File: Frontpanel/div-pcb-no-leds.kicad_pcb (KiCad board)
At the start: 2 copper layers, 20 x 128.5 mm, 0 parts

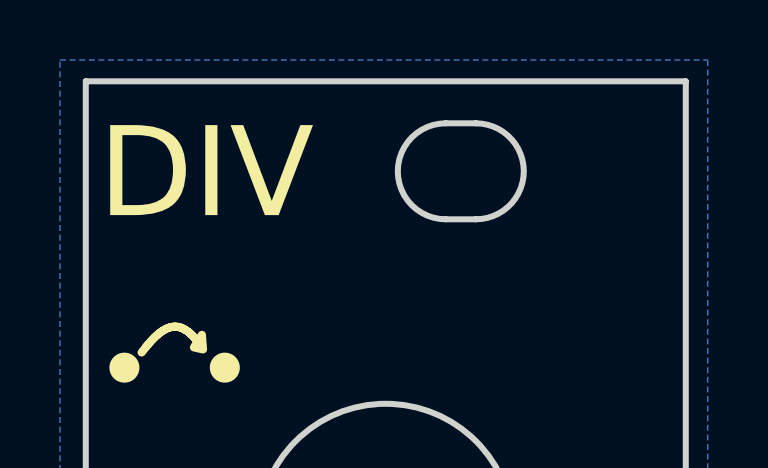
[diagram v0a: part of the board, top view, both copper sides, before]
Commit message: :lipstick: Change color of non-LED board and add "glow"
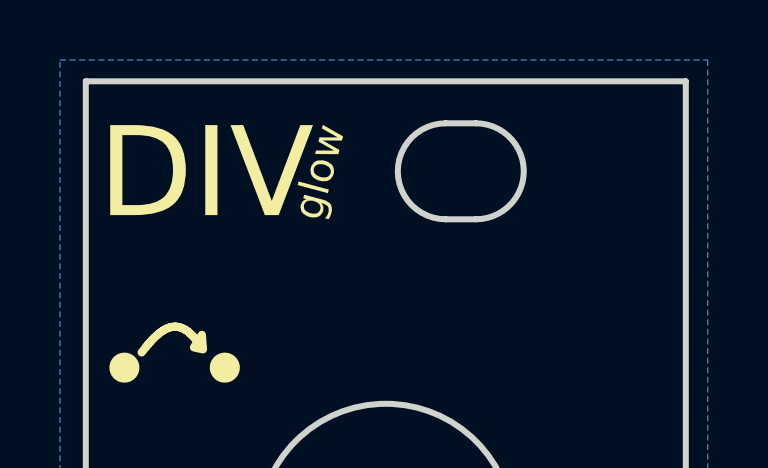
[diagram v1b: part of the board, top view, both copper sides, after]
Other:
- board text added: "glow"
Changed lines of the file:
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@@
   (setup
     (stackup
-      (layer "F.SilkS" (type "Top Silk Screen") (color "Black"))
+      (layer "F.SilkS" (type "Top Silk Screen") (color "White"))
       (layer "F.Paste" (type "Top Solder Paste"))
-      (layer "F.Mask" (type "Top Solder Mask") (color "White") (thickness 0.01))
+      (layer "F.Mask" (type "Top Solder Mask") (color "Black") (thickness 0.01))
       (layer "F.Cu" (type "copper") (thickness 0.035))
       (layer "dielectric 1" (type "core") (color "Polyimide") (thickness 1.51) (material "FR4") (epsilon_r 4.5) (loss_tangent 0.02))
       (layer "B.Cu" (type "copper") (thickness 0.035))
-      (layer "B.Mask" (type "Bottom Solder Mask") (color "White") (thickness 0.01))
+      (layer "B.Mask" (type "Bottom Solder Mask") (color "Black") (thickness 0.01))
       (layer "B.Paste" (type "Bottom Solder Paste"))
-      (layer "B.SilkS" (type "Bottom Silk Screen") (color "Black"))
+      (layer "B.SilkS" (type "Bottom Silk Screen") (color "White"))
       (copper_finish "None")
       (dielectric_constraints no)
@@
     (effects (font (size 2 2) (thickness 0.2)) (justify bottom))
   )
+  (gr_text "glow" (at 112.9284 39.7256 75) (layer "F.SilkS")
+    (effects (font (size 1 1) (thickness 0.1)) (justify left bottom))
+  )
   (zone (net 0) (net_name "") (layer "B.Cu") (hatch edge 0.5)

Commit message: :memo: Change frontpanel release to v1.1
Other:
- board text added: "v1.1"
- board text removed: "v1"
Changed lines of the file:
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@@
   (paper "A4")
   (title_block
-    (title "moPsy DIV (no LEDs)")
-    (date "2023-04-07")
-    (rev "v1")
+    (title "moPsy DIV glow (no LEDs)")
+    (date "2023-05-17")
+    (rev "v1.1")
   )
   (layers
@@
     (effects (font (size 2 2) (thickness 0.2)) (justify left bottom mirror))
   )
-  (gr_text "v1" (at 108.839 119.38 90) (layer "B.SilkS")
+  (gr_text "v1.1" (at 108.839 119.38 90) (layer "B.SilkS")
     (effects (font (size 2 2) (thickness 0.2)) (justify left bottom mirror))
   )
